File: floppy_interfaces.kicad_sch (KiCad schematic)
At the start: 24 parts, among them J13 Conn_01x04_Male, J14 Conn_02x17_Odd_Even, J16 Conn_01x04_Male, J6 SDF-60J for IEC 1541 serial p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, U1 74LS373, U2 74LVC374, U22 74LS06N, U3 74LVC374, U4 74LS373

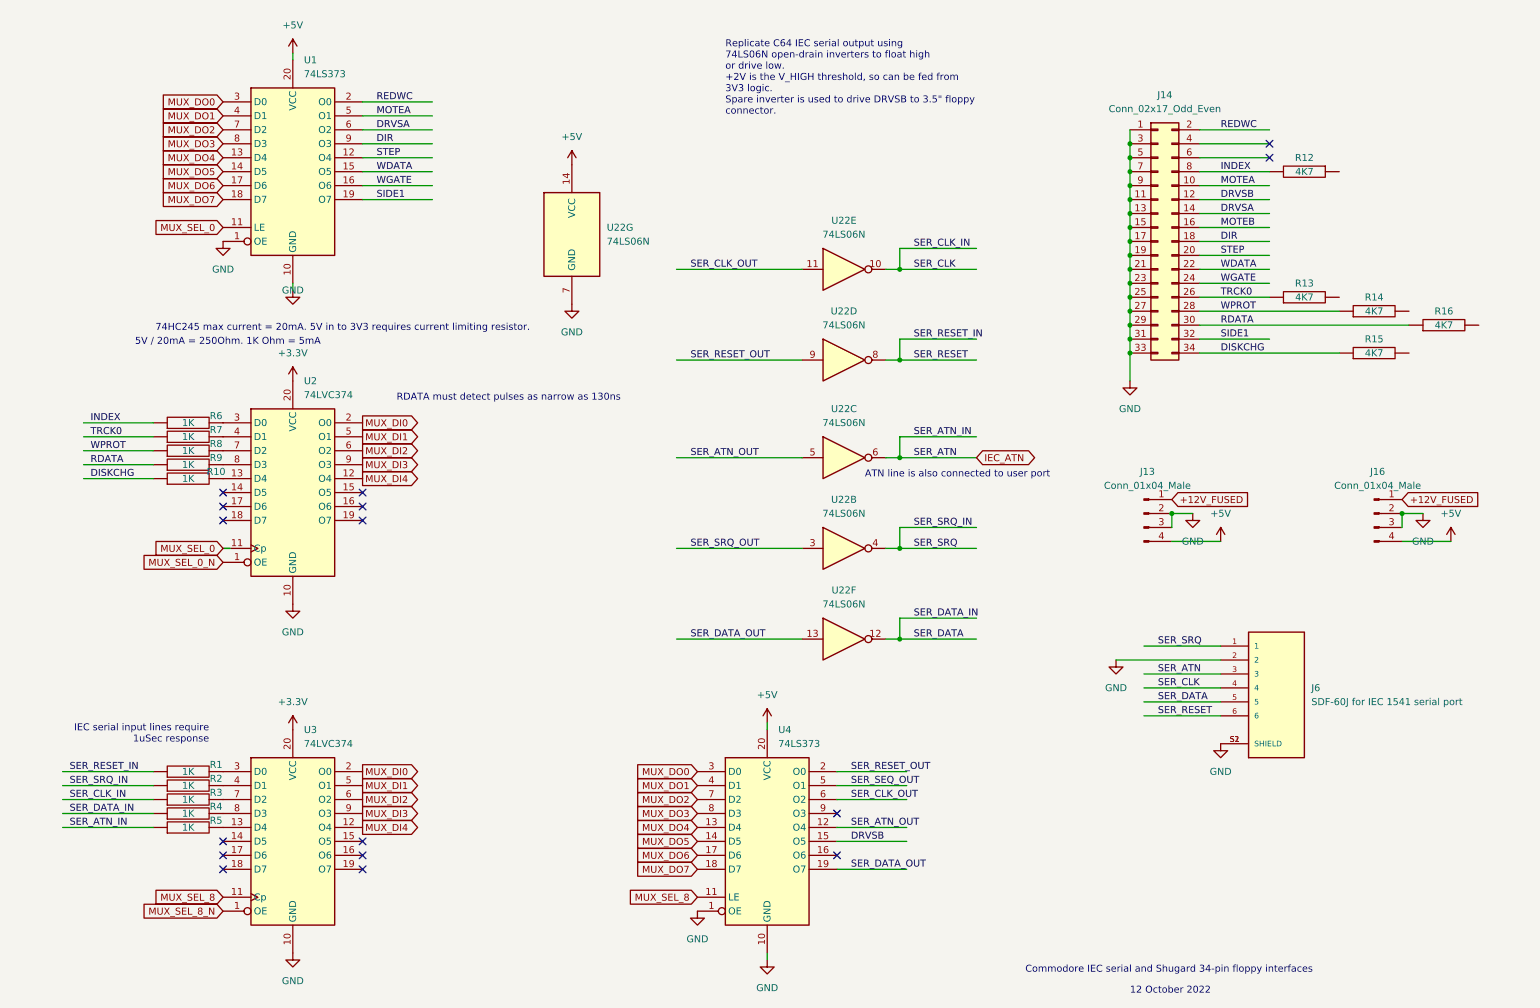
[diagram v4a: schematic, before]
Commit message: place floppy components and remove redundant resistors
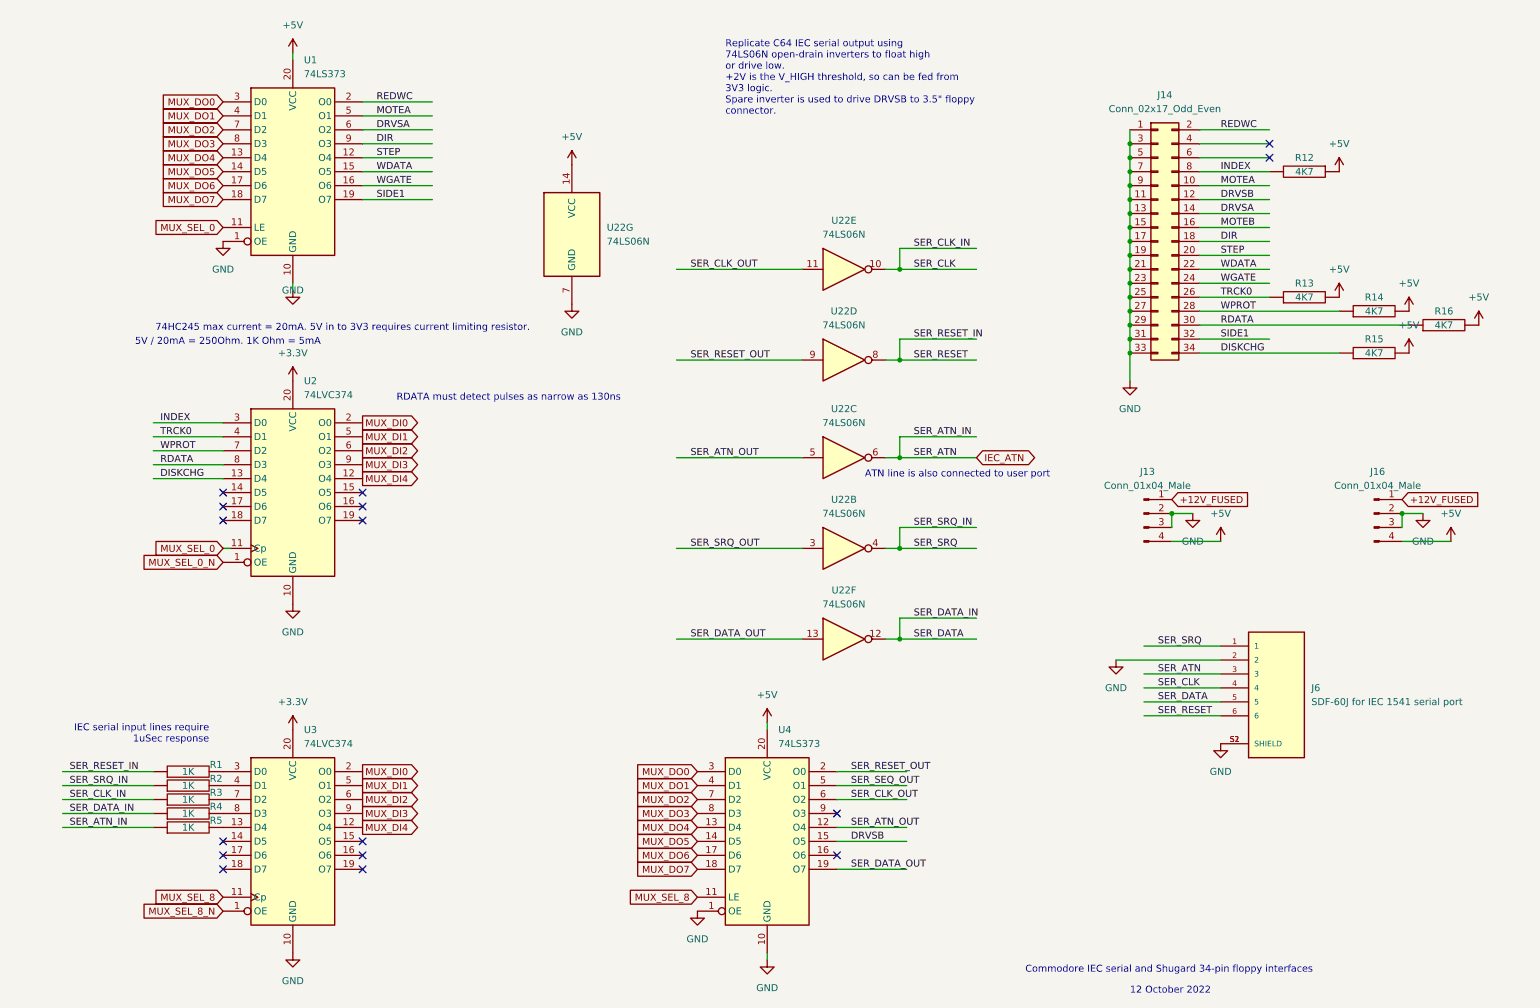
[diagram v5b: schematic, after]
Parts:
- removed R10, R6, R7, R8, R9: 1K, Resistor_THT:R_Box_L8.4mm_W2.5mm_P5.08mm, symbol pspice:R
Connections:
- net +5V: now also R12.1, R13.2, R14.2, R15.2, R16.2
- net DISKCHG: now also U2.13 (D4)
- net INDEX: now also U2.3 (D0)
- net RDATA: now also U2.8 (D3)
- net TRCK0: now also U2.4 (D1)
- net WPROT: now also U2.7 (D2)
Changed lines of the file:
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@@
     (stroke (width 0) (type default) (color 0 0 0 0))
   )
-  (wire (pts (xy 19.05 90.17) (xy 31.75 90.17))
+  (wire (pts (xy 31.75 90.17) (xy 44.45 90.17))
     (stroke (width 0) (type default) (color 0 0 0 0))
   )
@@
     (stroke (width 0) (type default) (color 0 0 0 0))
   )
-  (wire (pts (xy 19.05 100.33) (xy 31.75 100.33))
+  (wire (pts (xy 31.75 100.33) (xy 44.45 100.33))
     (stroke (width 0) (type default) (color 0 0 0 0))
   )
@@
     (stroke (width 0) (type default) (color 0 0 0 0))
   )
-  (wire (pts (xy 19.05 95.25) (xy 31.75 95.25))
+  (wire (pts (xy 31.75 95.25) (xy 44.45 95.25))
     (stroke (width 0) (type default) (color 0 0 0 0))
   )
@@
     (stroke (width 0) (type default) (color 0 0 0 0))
   )
-  (wire (pts (xy 19.05 97.79) (xy 31.75 97.79))
+  (wire (pts (xy 31.75 97.79) (xy 44.45 97.79))
     (stroke (width 0) (type default) (color 0 0 0 0))
   )
@@
     (stroke (width 0) (type default) (color 0 0 0 0))
   )
-  (wire (pts (xy 19.05 92.71) (xy 31.75 92.71))
+  (wire (pts (xy 31.75 92.71) (xy 44.45 92.71))
     (stroke (width 0) (type default) (color 0 0 0 0))
   )
@@
     (effects (font (size 1.27 1.27)) (justify left bottom))
   )
-  (label "RDATA" (at 20.32 97.79 0)
+  (label "RDATA" (at 33.02 97.79 0)
     (effects (font (size 1.27 1.27)) (justify left bottom))
   )
@@
     (effects (font (size 1.27 1.27)) (justify left bottom))
   )
-  (label "WPROT" (at 20.32 95.25 0)
+  (label "WPROT" (at 33.02 95.25 0)
     (effects (font (size 1.27 1.27)) (justify left bottom))
   )
@@
     (effects (font (size 1.27 1.27)) (justify left bottom))
   )
-  (label "TRCK0" (at 20.32 92.71 0)
+  (label "TRCK0" (at 33.02 92.71 0)
     (effects (font (size 1.27 1.27)) (justify left bottom))
   )
@@
     (effects (font (size 1.27 1.27)) (justify left bottom))
   )
-  (label "DISKCHG" (at 20.32 100.33 0)
+  (label "DISKCHG" (at 33.02 100.33 0)
     (effects (font (size 1.27 1.27)) (justify left bottom))
   )
@@
     (effects (font (size 1.27 1.27)) (justify left bottom))
   )
-  (label "INDEX" (at 20.32 90.17 0)
+  (label "INDEX" (at 33.02 90.17 0)
     (effects (font (size 1.27 1.27)) (justify left bottom))
   )
@@
     (pin "7")
   )
+  (symbol (lib_id "power:+5V") (at 260.35 77.47 0) (unit 1)
+    (in_bom yes) (on_board yes) (fields_autoplaced)
+    (property "Reference" "#PWR?" (id 0) (at 260.35 81.28 0)
+      (effects (font (size 1.27 1.27)) hide)
+    )
+    (property "Value" "+5V" (id 1) (at 260.35 72.39 0))
+    (property "Footprint" "" (id 2) (at 260.35 77.47 0)
+      (effects (font (size 1.27 1.27)) hide)
+    )
+    (property "Datasheet" "" (id 3) (at 260.35 77.47 0)
+      (effects (font (size 1.27 1.27)) hide)
+    )
+    (pin "1")
+  )
   (symbol (lib_id "pspice:R") (at 38.1 156.21 90) (unit 1)
     (in_bom yes) (on_board yes)
@@
     (pin "2")
   )
-  (symbol (lib_id "pspice:R") (at 38.1 95.25 90) (unit 1)
-    (in_bom yes) (on_board yes)
-    (property "Reference" "R8" (id 0) (at 43.18 93.98 90))
-    (property "Value" "1K" (id 1) (at 38.1 95.25 90))
-    (property "Footprint" "Resistor_THT:R_Box_L8.4mm_W2.5mm_P5.08mm" (id 2) (at 38.1 95.25 0)
-      (effects (font (size 1.27 1.27)) hide)
-    )
-    (property "Datasheet" "~" (id 3) (at 38.1 95.25 0)
-      (effects (font (size 1.27 1.27)) hide)
-    )
-    (pin "1")
-    (pin "2")
+  (symbol (lib_id "power:+5V") (at 247.65 67.31 0) (unit 1)
+    (in_bom yes) (on_board yes) (fields_autoplaced)
+    (property "Reference" "#PWR?" (id 0) (at 247.65 71.12 0)
+      (effects (font (size 1.27 1.27)) hide)
+    )
+    (property "Value" "+5V" (id 1) (at 247.65 62.23 0))
+    (property "Footprint" "" (id 2) (at 247.65 67.31 0)
+      (effects (font (size 1.27 1.27)) hide)
+    )
+    (property "Datasheet" "" (id 3) (at 247.65 67.31 0)
+      (effects (font (size 1.27 1.27)) hide)
+    )
+    (pin "1")
   )
   (symbol (lib_id "Connector_Generic:Conn_02x17_Odd_Even") (at 214.63 57.15 0) (unit 1)
@@
     (pin "1")
   )
+  (symbol (lib_id "power:+5V") (at 273.05 72.39 0) (unit 1)
+    (in_bom yes) (on_board yes) (fields_autoplaced)
+    (property "Reference" "#PWR?" (id 0) (at 273.05 76.2 0)
+      (effects (font (size 1.27 1.27)) hide)
+    )
+    (property "Value" "+5V" (id 1) (at 273.05 67.31 0))
+    (property "Footprint" "" (id 2) (at 273.05 72.39 0)
+      (effects (font (size 1.27 1.27)) hide)
+    )
+    (property "Datasheet" "" (id 3) (at 273.05 72.39 0)
+      (effects (font (size 1.27 1.27)) hide)
+    )
+    (pin "1")
+  )
   (symbol (lib_id "Connector:Conn_01x04_Male") (at 254 106.68 0) (unit 1)
     (in_bom yes) (on_board yes) (fields_autoplaced)
@@
     (pin "9")
   )
-  (symbol (lib_id "pspice:R") (at 38.1 92.71 90) (unit 1)
-    (in_bom yes) (on_board yes)
-    (property "Reference" "R7" (id 0) (at 43.18 91.44 90))
-    (property "Value" "1K" (id 1) (at 38.1 92.71 90))
-    (property "Footprint" "Resistor_THT:R_Box_L8.4mm_W2.5mm_P5.08mm" (id 2) (at 38.1 92.71 0)
-      (effects (font (size 1.27 1.27)) hide)
-    )
-    (property "Datasheet" "~" (id 3) (at 38.1 92.71 0)
-      (effects (font (size 1.27 1.27)) hide)
-    )
-    (pin "1")
-    (pin "2")
+  (symbol (lib_id "power:+5V") (at 247.65 44.45 0) (unit 1)
+    (in_bom yes) (on_board yes) (fields_autoplaced)
+    (property "Reference" "#PWR?" (id 0) (at 247.65 48.26 0)
+      (effects (font (size 1.27 1.27)) hide)
+    )
+    (property "Value" "+5V" (id 1) (at 247.65 39.37 0))
+    (property "Footprint" "" (id 2) (at 247.65 44.45 0)
+      (effects (font (size 1.27 1.27)) hide)
+    )
+    (property "Datasheet" "" (id 3) (at 247.65 44.45 0)
+      (effects (font (size 1.27 1.27)) hide)
+    )
+    (pin "1")
   )
   (symbol (lib_id "power:GND") (at 207.01 133.35 0) (unit 1)
@@
     (pin "9")
   )
-  (symbol (lib_id "pspice:R") (at 38.1 97.79 90) (unit 1)
-    (in_bom yes) (on_board yes)
-    (property "Reference" "R9" (id 0) (at 43.18 96.52 90))
-    (property "Value" "1K" (id 1) (at 38.1 97.79 90))
-    (property "Footprint" "Resistor_THT:R_Box_L8.4mm_W2.5mm_P5.08mm" (id 2) (at 38.1 97.79 0)
-      (effects (font (size 1.27 1.27)) hide)
-    )
-    (property "Datasheet" "~" (id 3) (at 38.1 97.79 0)
-      (effects (font (size 1.27 1.27)) hide)
-    )
-    (pin "1")
-    (pin "2")
-  )
   (symbol (lib_id "74xx:74HC374") (at 57.15 102.87 0) (unit 1)
     (in_bom yes) (on_board yes) (fields_autoplaced)
@@
     (pin "2")
   )
-  (symbol (lib_id "pspice:R") (at 38.1 90.17 90) (unit 1)
-    (in_bom yes) (on_board yes)
-    (property "Reference" "R6" (id 0) (at 43.18 88.9 90))
-    (property "Value" "1K" (id 1) (at 38.1 90.17 90))
-    (property "Footprint" "Resistor_THT:R_Box_L8.4mm_W2.5mm_P5.08mm" (id 2) (at 38.1 90.17 0)
-      (effects (font (size 1.27 1.27)) hide)
-    )
-    (property "Datasheet" "~" (id 3) (at 38.1 90.17 0)
-      (effects (font (size 1.27 1.27)) hide)
-    )
-    (pin "1")
-    (pin "2")
-  )
   (symbol (lib_id "74xx:74LS06N") (at 157.48 129.54 0) (unit 6)
     (in_bom yes) (on_board yes) (fields_autoplaced)
@@
     (pin "1")
   )
-  (symbol (lib_id "pspice:R") (at 38.1 100.33 90) (unit 1)
-    (in_bom yes) (on_board yes)
-    (property "Reference" "R10" (id 0) (at 43.18 99.06 90))
-    (property "Value" "1K" (id 1) (at 38.1 100.33 90))
-    (property "Footprint" "Resistor_THT:R_Box_L8.4mm_W2.5mm_P5.08mm" (id 2) (at 38.1 100.33 0)
-      (effects (font (size 1.27 1.27)) hide)
-    )
-    (property "Datasheet" "~" (id 3) (at 38.1 100.33 0)
-      (effects (font (size 1.27 1.27)) hide)
-    )
-    (pin "1")
-    (pin "2")
+  (symbol (lib_id "power:+5V") (at 260.35 69.85 0) (unit 1)
+    (in_bom yes) (on_board yes) (fields_autoplaced)
+    (property "Reference" "#PWR?" (id 0) (at 260.35 73.66 0)
+      (effects (font (size 1.27 1.27)) hide)
+    )
+    (property "Value" "+5V" (id 1) (at 260.35 64.77 0))
+    (property "Footprint" "" (id 2) (at 260.35 69.85 0)
+      (effects (font (size 1.27 1.27)) hide)
+    )
+    (property "Datasheet" "" (id 3) (at 260.35 69.85 0)
+      (effects (font (size 1.27 1.27)) hide)
+    )
+    (pin "1")
   )
   (symbol (lib_id "power:GND") (at 57.15 66.04 0) (unit 1)

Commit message: switch DIP8 to DIP4 using spare pins on floppy MUX R unit
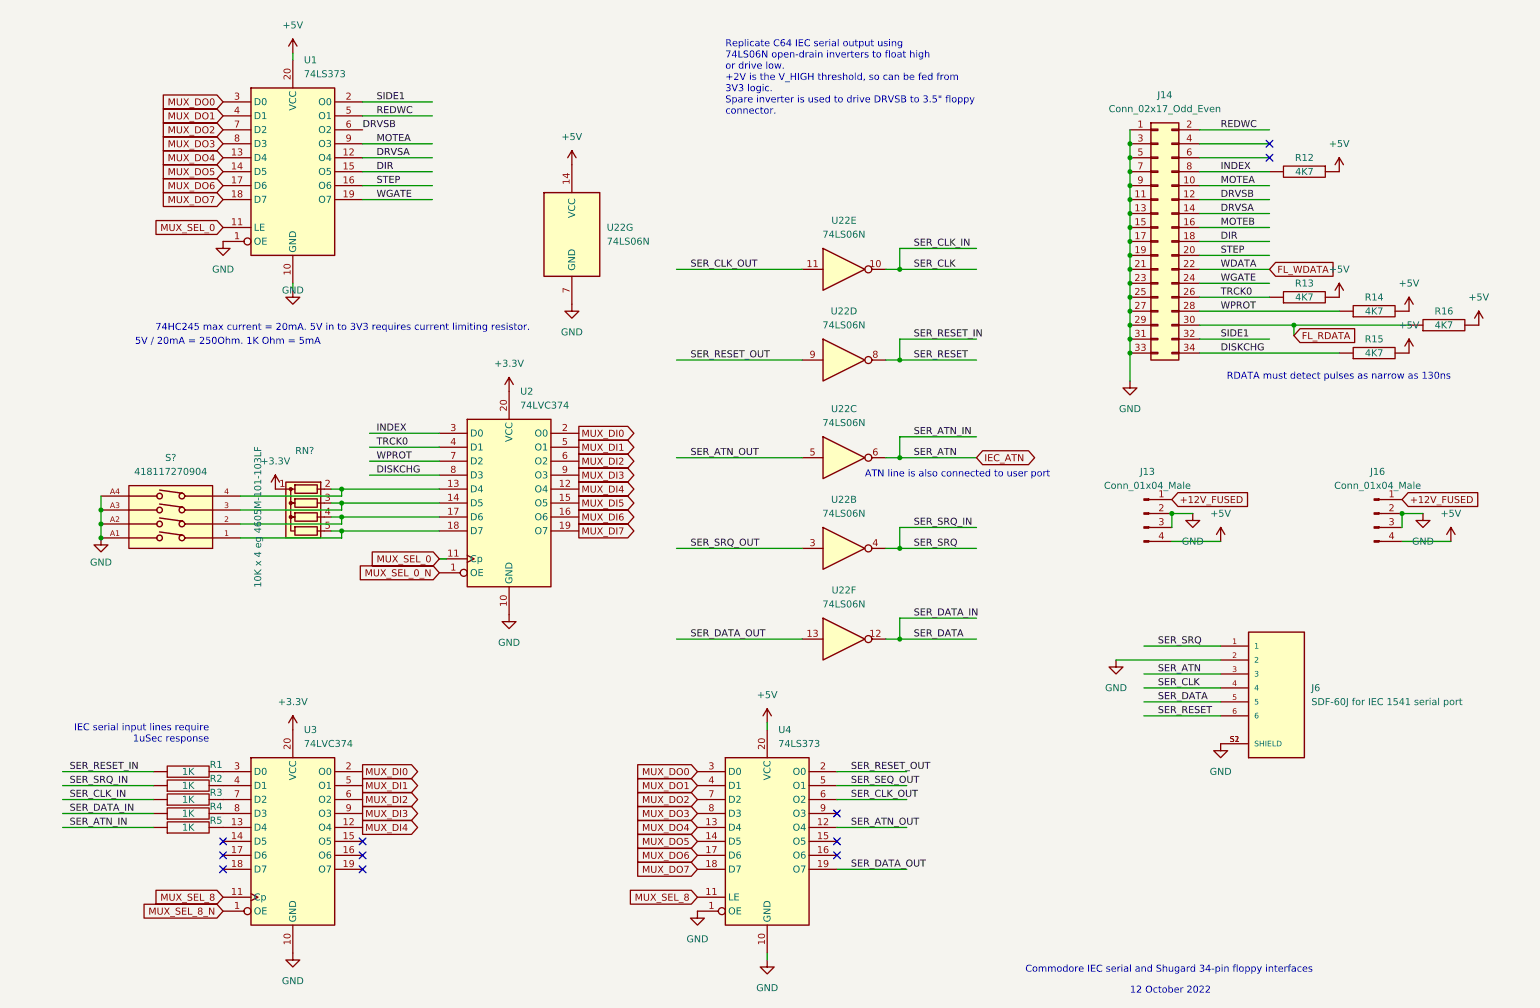
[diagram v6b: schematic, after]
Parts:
- added RN?: 10K x 4 eg 4605M-101-103LF, Resistor_THT:R_Array_SIP5, symbol Device:R_Network04
- added S?: 418117270904, 418117270904, symbol 00Project-DIP-SW-4:418117270904
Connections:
- net +3V3: now also RN?.1 (common)
- net DIR: now also U1.15 (O5); no longer U1.9 (O3)
- net DISKCHG: now also U2.8 (D3); no longer U2.13 (D4)
- net DRVSA: now also U1.12 (O4); no longer U1.6 (O2)
- net DRVSB: now also U1.6 (O2); no longer U4.15 (O5)
- net GND: now also S?.A1, S?.A2, S?.A3, S?.A4
- net MOTEA: now also U1.9 (O3); no longer U1.5 (O1)
- net REDWC: now also U1.5 (O1); no longer U1.2 (O0)
- net SIDE1: now also U1.2 (O0); no longer U1.19 (O7)
- net STEP: now also U1.16 (O6); no longer U1.12 (O4)
- net WGATE: now also U1.19 (O7); no longer U1.16 (O6)
- net at U2.14 (D5): now also RN?.3 (R2), S?.3
- net MUX_DI5: now reaches U2.15 (O5)
- net MUX_DI6: now reaches U2.16 (O6)
- net at U2.17 (D6): now also RN?.4 (R3), S?.2
- net at U2.18 (D7): now also RN?.5 (R4), S?.1
- net MUX_DI7: now reaches U2.19 (O7)
- net RDATA renamed FL_RDATA
- net FL_RDATA: no longer U2.8 (D3)
- net WDATA renamed FL_WDATA
- net FL_WDATA: no longer U1.15 (O5)
- new net: RN?.2 (R1), S?.4, U2.13 (D4)
- no-connect marks 16 -> 11
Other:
- moved on the sheet: U2
